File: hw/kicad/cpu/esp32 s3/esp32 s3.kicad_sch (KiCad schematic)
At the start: 40 parts, among them J1 TOP, J2 BUTTOM, J3 USB_B_Micro, SW1 SW_Push, U1 ESP32-S3-WROOM-1-N16R2, U2 ICM-42688-P

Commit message: 尽力改成40mmx40mm
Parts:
- added R19: 1k, Resistor_SMD:R_0805_2012Metric, symbol Device:R
- added R20, R31: 100, Resistor_SMD:R_0603_1608Metric, symbol Device:R
- added SW2: SW_Push, Button_Switch_THT:SW_SPST_Omron_B3F-315x_Angled, symbol Switch:SW_Push
- SW1: footprint Button_Switch_SMD:SW_DIP_SPSTx01_Slide_6.7x4.1mm_W6.73mm_P2.54mm_LowProfile_JPin -> Button_Switch_THT:SW_SPST_Omron_B3F-315x_Angled
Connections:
- net UART1_RX is gone; now on net UART1_Rx: R7.2
- net UART1_TX is gone; now on net UART1_Tx: R8.2
- net UART2_RX is gone; now on net UART2_Rx: R9.2
- net UART2_TX is gone; now on net UART2_Tx: R10.2
- net UART3_Rx is gone; now on net I2C_SDA: J1.9 (Pin_9), J2.10 (Pin_10)
- net UART3_Tx is gone; now on net I2C_CLK: J1.10 (Pin_10), J2.9 (Pin_9)
- net usb_d+ is gone; now on net usb+: U1.14 (IO20)
- net usb_d- is gone; now on net usb-: U1.13 (IO19)
- net GND: now also R19.1
- net GPIO_1: now also J1.15 (Pin_15), J2.16 (Pin_16); no longer J1.17 (Pin_17), J2.18 (Pin_18)
- net GPIO_10: now also J1.24 (Pin_24), J2.23 (Pin_23); no longer J1.26 (Pin_26), J2.25 (Pin_25)
- net GPIO_2: now also J1.16 (Pin_16), J2.15 (Pin_15); no longer J1.18 (Pin_18), J2.17 (Pin_17)
- net GPIO_3: now also J1.17 (Pin_17), J2.18 (Pin_18); no longer J1.19 (Pin_19), J2.20 (Pin_20)
- net GPIO_4: now also J1.18 (Pin_18), J2.17 (Pin_17); no longer J1.20 (Pin_20), J2.19 (Pin_19)
- net GPIO_5: now also J1.19 (Pin_19), J2.20 (Pin_20); no longer J1.21 (Pin_21), J2.22 (Pin_22)
- net GPIO_6: now also J1.20 (Pin_20), J2.19 (Pin_19); no longer J1.22 (Pin_22), J2.21 (Pin_21)
- net GPIO_7: now also J1.21 (Pin_21), J2.22 (Pin_22); no longer J1.23 (Pin_23), J2.24 (Pin_24)
- net GPIO_8: now also J1.22 (Pin_22), J2.21 (Pin_21); no longer J1.24 (Pin_24), J2.23 (Pin_23)
- net GPIO_9: now also J1.23 (Pin_23), J2.24 (Pin_24); no longer J1.25 (Pin_25), J2.26 (Pin_26)
- net I2C_CLK: no longer J1.12 (Pin_12), J2.11 (Pin_11)
- net I2C_SDA: no longer J1.11 (Pin_11), J2.12 (Pin_12)
- net IMU_FSYNC: now also U1.20 (IO12); no longer U1.25 (IO48)
- net SPI_CLK: now also J1.12 (Pin_12), J2.11 (Pin_11); no longer J1.14 (Pin_14), J2.13 (Pin_13)
- net SPI_CS: now also J1.11 (Pin_11), J2.12 (Pin_12); no longer J1.13 (Pin_13), J2.14 (Pin_14)
- net SPI_MISO: now also J1.14 (Pin_14), J2.13 (Pin_13); no longer J1.16 (Pin_16), J2.15 (Pin_15)
- net SPI_MOSI: now also J1.13 (Pin_13), J2.14 (Pin_14); no longer J1.15 (Pin_15), J2.16 (Pin_16)
- net gpio1: now also U1.24 (IO47); no longer U1.28 (IO35)
- net gpio10: now also U1.35 (IO42); no longer U1.39 (IO1)
- net gpio2: now also U1.25 (IO48); no longer U1.29 (IO36)
- net gpio3: now also U1.28 (IO35); no longer U1.30 (IO37)
- net gpio4: now also U1.29 (IO36); no longer U1.31 (IO38)
- net gpio5: now also U1.30 (IO37); no longer R26.1, U1.32 (IO39), U1.33 (IO40)
- net gpio7: now also U1.32 (IO39); no longer U1.34 (IO41)
- net gpio8: now also U1.33 (IO40); no longer U1.35 (IO42)
- net gpio9: now also U1.34 (IO41); no longer U1.38 (IO2)
- net i2c_clk: now also R12.1, U1.11 (IO18); no longer R11.1, U1.10 (IO17)
- net i2c_sda: now also R11.1, U1.10 (IO17); no longer R12.1, U1.11 (IO18)
- net spi2_clk: now also R14.1, U1.18 (IO10); no longer U1.19 (IO11)
- net spi2_cs: now also R13.1, U1.16 (IO46); no longer U1.17 (IO9)
- net spi2_miso: now also R16.1, U1.15 (IO3); no longer U1.20 (IO12)
- net spi2_mosi: now also R15.1, U1.17 (IO9); no longer U1.18 (IO10)
- net spi3_clk: no longer R14.1
- net spi3_cs: no longer R13.1
- net spi3_miso: now also U1.19 (IO11); no longer R16.1, U1.24 (IO47)
- net spi3_mosi: no longer R15.1
- net uart1_rx: now also U1.8 (IO15); no longer U1.9 (IO16)
- net uart1_tx: now also U1.9 (IO16); no longer U1.8 (IO15)
- net at U1.26 (IO45): now also SW2.2
- net USB+ renamed usb+
- net USB- renamed usb-
- new net: R19.2, SW2.1
- new net GPIO_11: J1.25 (Pin_25), J2.26 (Pin_26), R20.2
- new net GPIO_12: J1.26 (Pin_26), J2.25 (Pin_25), R31.2
- new net gpio11: R20.1, U1.38 (IO2)
- new net gpio12: R31.1, U1.39 (IO1)
- new net gpio6: R26.1, U1.31 (IO38)
- no-connect marks 5 -> 2
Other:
- note added: "烧录固件时，长按sw1调用esp_restart重启至boot模式，刚好io0此时也拉低"
- moved on the sheet: R1, SW1, U1

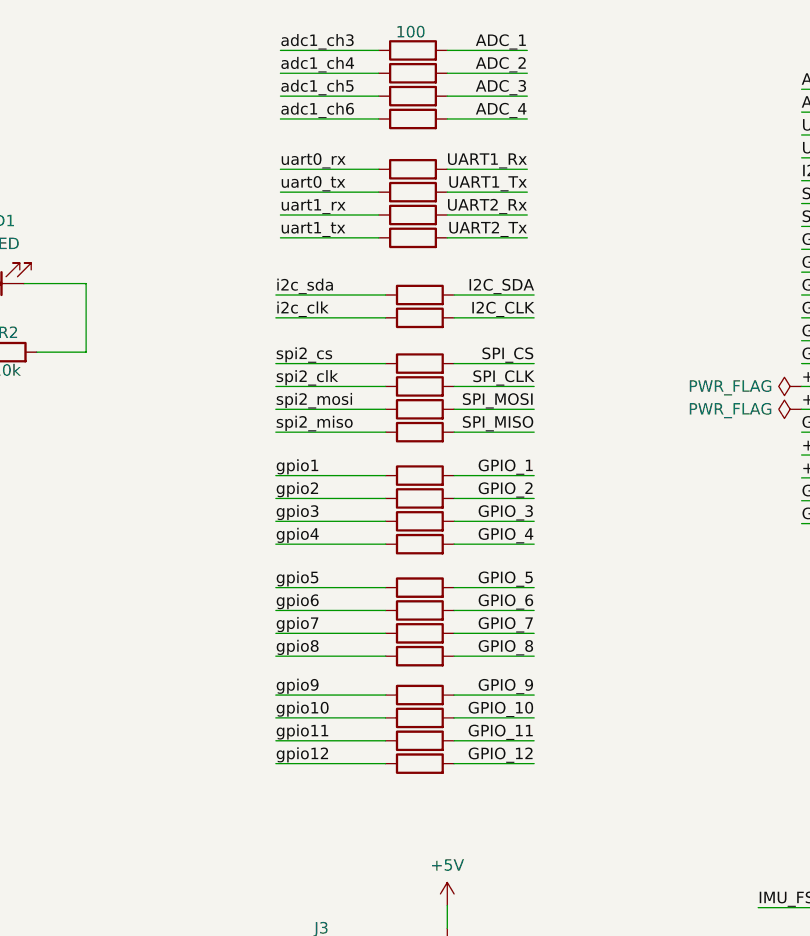
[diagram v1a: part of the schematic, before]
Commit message: esp32部分该小板框可太难了，小电阻太多，只好全部去掉。
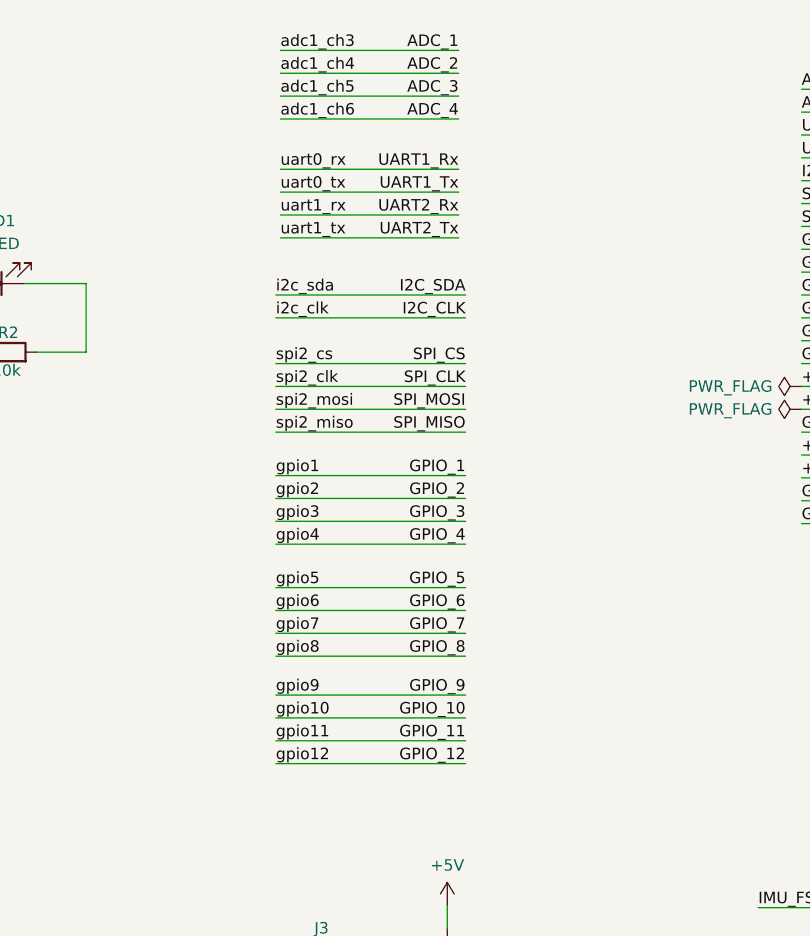
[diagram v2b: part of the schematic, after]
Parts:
- removed R10, R11, R12, R13, R14, R15, R16, R17, R18, R20, R21, R22, R23, R24, R25, R26, R27, R28, R3, R31, R4, R5, R6, R7, R8, R9: 100, Resistor_SMD:R_0603_1608Metric, symbol Device:R
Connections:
- net adc1_ch3 is gone; now on net ADC_1: U1.4 (IO4)
- net adc1_ch4 is gone; now on net ADC_2: U1.5 (IO5)
- net adc1_ch5 is gone; now on net ADC_3: U1.6 (IO6)
- net adc1_ch6 is gone; now on net ADC_4: U1.7 (IO7)
- net gpio1 is gone; now on net GPIO_1: U1.24 (IO47)
- net gpio10 is gone; now on net GPIO_10: U1.35 (IO42)
- net gpio11 is gone; now on net GPIO_11: U1.38 (IO2)
- net gpio12 is gone; now on net GPIO_12: U1.39 (IO1)
- net gpio2 is gone; now on net GPIO_2: U1.25 (IO48)
- net gpio3 is gone; now on net GPIO_3: U1.28 (IO35)
- net gpio4 is gone; now on net GPIO_4: U1.29 (IO36)
- net gpio5 is gone; now on net GPIO_5: U1.30 (IO37)
- net gpio6 is gone; now on net GPIO_6: U1.31 (IO38)
- net gpio7 is gone; now on net GPIO_7: U1.32 (IO39)
- net gpio8 is gone; now on net GPIO_8: U1.33 (IO40)
- net gpio9 is gone; now on net GPIO_9: U1.34 (IO41)
- net i2c_clk is gone; now on net I2C_CLK: U1.11 (IO18)
- net i2c_sda is gone; now on net I2C_SDA: U1.10 (IO17)
- net spi2_clk is gone; now on net SPI_CLK: U1.18 (IO10)
- net spi2_cs is gone; now on net SPI_CS: U1.16 (IO46)
- net spi2_miso is gone; now on net SPI_MISO: U1.15 (IO3)
- net spi2_mosi is gone; now on net SPI_MOSI: U1.17 (IO9)
- net uart0_rx is gone; now on net UART1_Rx: U1.36 (RXD0)
- net uart0_tx is gone; now on net UART1_Tx: U1.37 (TXD0)
- net uart1_rx is gone; now on net UART2_Rx: U1.8 (IO15)
- net uart1_tx is gone; now on net UART2_Tx: U1.9 (IO16)

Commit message: Merge from normal
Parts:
- removed SW2: SW_Push, Button_Switch_THT:SW_SPST_Omron_B3F-315x_Angled, symbol Switch:SW_Push
- added R10, R11, R12, R13, R14, R15, R16, R17, R18, R20, R21, R22, R23, R24, R25, R26, R27, R28, R3, R4, R5, R6, R7, R8, R9: R, Resistor_SMD:R_0603_1608Metric, symbol Device:R
- R1, R29, R30: footprint Resistor_SMD:R_0805_2012Metric -> Resistor_SMD:R_0603_1608Metric
- R19: value 1k -> R; footprint Resistor_SMD:R_0805_2012Metric -> Resistor_SMD:R_0603_1608Metric
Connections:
- net ADC_1: now also R3.2; no longer U1.4 (IO4)
- net ADC_2: now also R4.2; no longer U1.5 (IO5)
- net ADC_3: now also R5.2; no longer U1.6 (IO6)
- net ADC_4: now also R6.2; no longer U1.7 (IO7)
- net GND: now also SW1.1, U1.41_10 (GND), U1.41_11 (GND), U1.41_12 (GND), U1.41_13 (GND), U1.41_14 (GND), U1.41_15 (GND), U1.41_16 (GND), U1.41_17 (GND), U1.41_18 (GND), U1.41_19 (GND), U1.41_20 (GND), U1.41_21 (GND); no longer R1.1, R19.1
- net GPIO_1: now also R17.2; no longer U1.24 (IO47)
- net GPIO_10: now also R26.2; no longer U1.35 (IO42)
- net GPIO_11: now also R27.2; no longer U1.38 (IO2)
- net GPIO_12: now also R28.2; no longer U1.39 (IO1)
- net GPIO_2: now also R18.2; no longer U1.25 (IO48)
- net GPIO_3: now also R19.2; no longer U1.28 (IO35)
- net GPIO_4: now also R20.2; no longer U1.29 (IO36)
- net GPIO_5: now also R21.2; no longer U1.30 (IO37)
- net GPIO_6: now also R22.2; no longer U1.31 (IO38)
- net GPIO_7: now also R23.2; no longer U1.32 (IO39)
- net GPIO_8: now also R24.2; no longer U1.33 (IO40)
- net GPIO_9: now also R25.2; no longer U1.34 (IO41)
- net I2C_CLK: now also R12.2; no longer U1.11 (IO18)
- net I2C_SDA: now also R11.2; no longer U1.10 (IO17)
- net IMU_FSYNC: now also U1.23 (IO21); no longer U1.20 (IO12)
- net LED: now also U1.24 (IO47); no longer U1.12 (IO8)
- net SPI_CLK: now also R14.2; no longer U1.18 (IO10)
- net SPI_CS: now also R13.2; no longer U1.16 (IO46)
- net SPI_MISO: now also R16.2; no longer U1.15 (IO3)
- net SPI_MOSI: now also R15.2; no longer U1.17 (IO9)
- net UART1_Rx: now also R7.2; no longer U1.36 (RXD0)
- net UART1_Tx: now also R8.2; no longer U1.37 (TXD0)
- net UART2_Rx: now also R9.2; no longer U1.8 (IO15)
- net UART2_Tx: now also R10.2; no longer U1.9 (IO16)
- net spi3_clk: now also U1.16 (IO46), R14.1; no longer U1.22 (IO14), U2.13 (AP_SCL/AP_SCLK)
- net spi3_cs: now also U1.15 (IO3), R13.1; no longer U1.21 (IO13), U2.12 (AP_CS)
- net spi3_miso: now also U1.18 (IO10), R16.1; no longer U1.19 (IO11), U2.1 (AP_SDO/AP_AD0)
- net spi3_mosi: now also U1.17 (IO9), R15.1; no longer U1.23 (IO21), U2.14 (AP_SDA/AP_SDIO/AP_SDI)
- net gpio2: now reaches U1.26 (IO45)
- net gpio2: now also R18.1
- net at U1.27 (IO0): now also R1.2; no longer SW1.2
- new net: R1.1, SW1.2
- new net adc1_ch3: R3.1, U1.4 (IO4)
- new net adc1_ch4: R4.1, U1.5 (IO5)
- new net adc1_ch5: R5.1, U1.6 (IO6)
- new net adc1_ch6: R6.1, U1.7 (IO7)
- new net gpio1: R17.1, U1.25 (IO48)
- new net gpio10: R26.1, U1.35 (IO42)
- new net gpio11: R27.1, U1.38 (IO2)
- new net gpio12: R28.1, U1.39 (IO1)
- new net gpio3: R19.1, U1.28 (IO35)
- new net gpio4: R20.1, U1.29 (IO36)
- new net gpio5: R21.1, U1.30 (IO37)
- new net gpio6: R22.1, U1.31 (IO38)
- new net gpio7: R23.1, U1.32 (IO39)
- new net gpio8: R24.1, U1.33 (IO40)
- new net gpio9: R25.1, U1.34 (IO41)
- new net i2c_clk: R12.1, U1.11 (IO18)
- new net i2c_sda: R11.1, U1.10 (IO17)
- new net spi2_clk: U1.21 (IO13), U2.13 (AP_SCL/AP_SCLK)
- new net spi2_cs: U1.22 (IO14), U2.12 (AP_CS)
- new net spi2_miso: U1.19 (IO11), U2.1 (AP_SDO/AP_AD0)
- new net spi2_mosi: U1.20 (IO12), U2.14 (AP_SDA/AP_SDIO/AP_SDI)
- new net uart0_rx: R7.1, U1.36 (RXD0)
- new net uart0_tx: R8.1, U1.37 (TXD0)
- new net uart1_rx: R9.1, U1.8 (IO15)
- new net uart1_tx: R10.1, U1.9 (IO16)
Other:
- moved on the sheet: R1, SW1
